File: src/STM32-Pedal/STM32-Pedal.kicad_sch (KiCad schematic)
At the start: 15 parts, among them J1 AudioJack2, U1 OPA134, U2 OPA134, U3 STM32H743ZITx

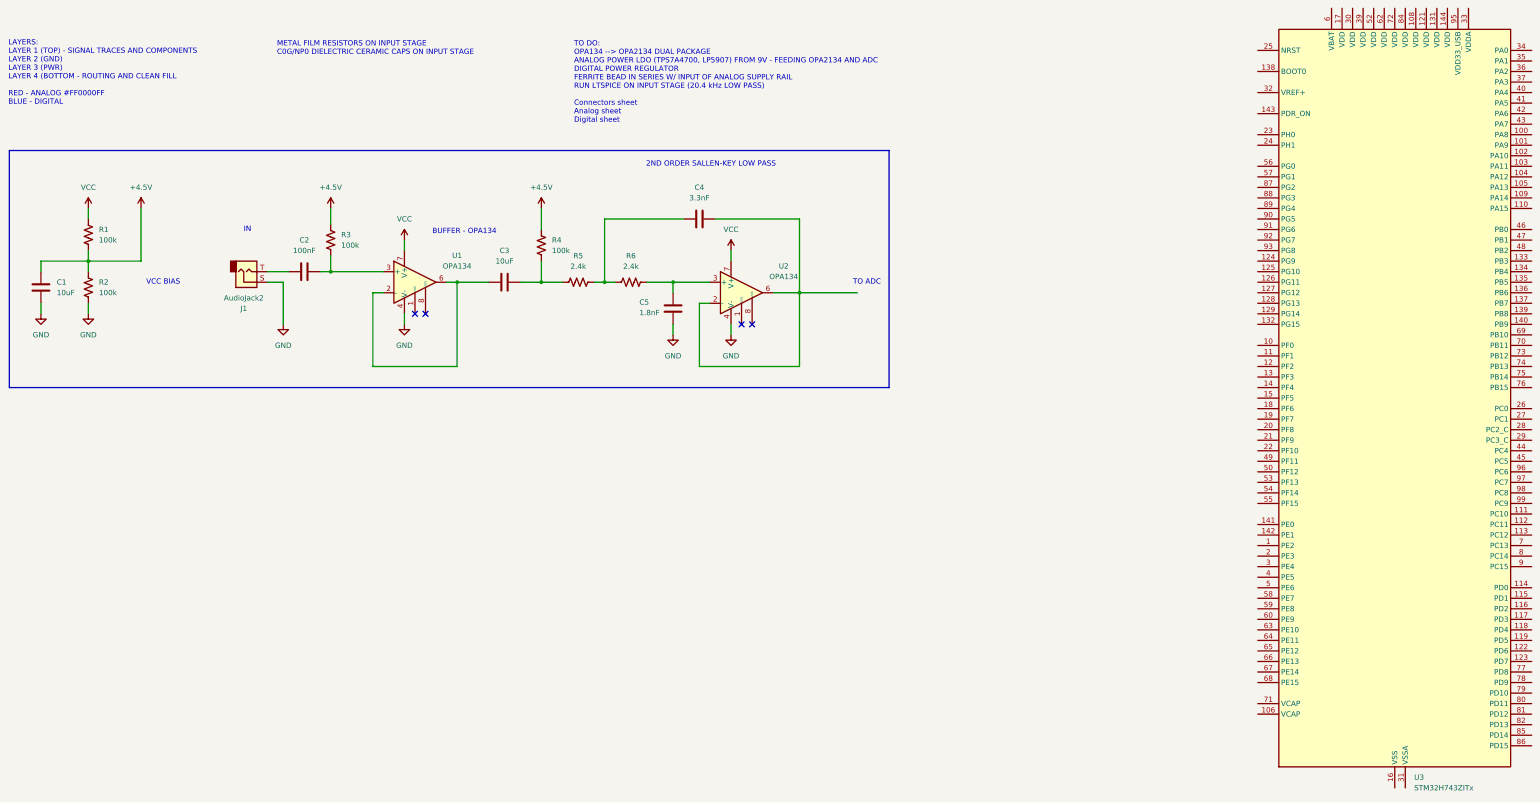
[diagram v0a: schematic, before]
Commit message: Schematic: codec, power, hierarchical sheets
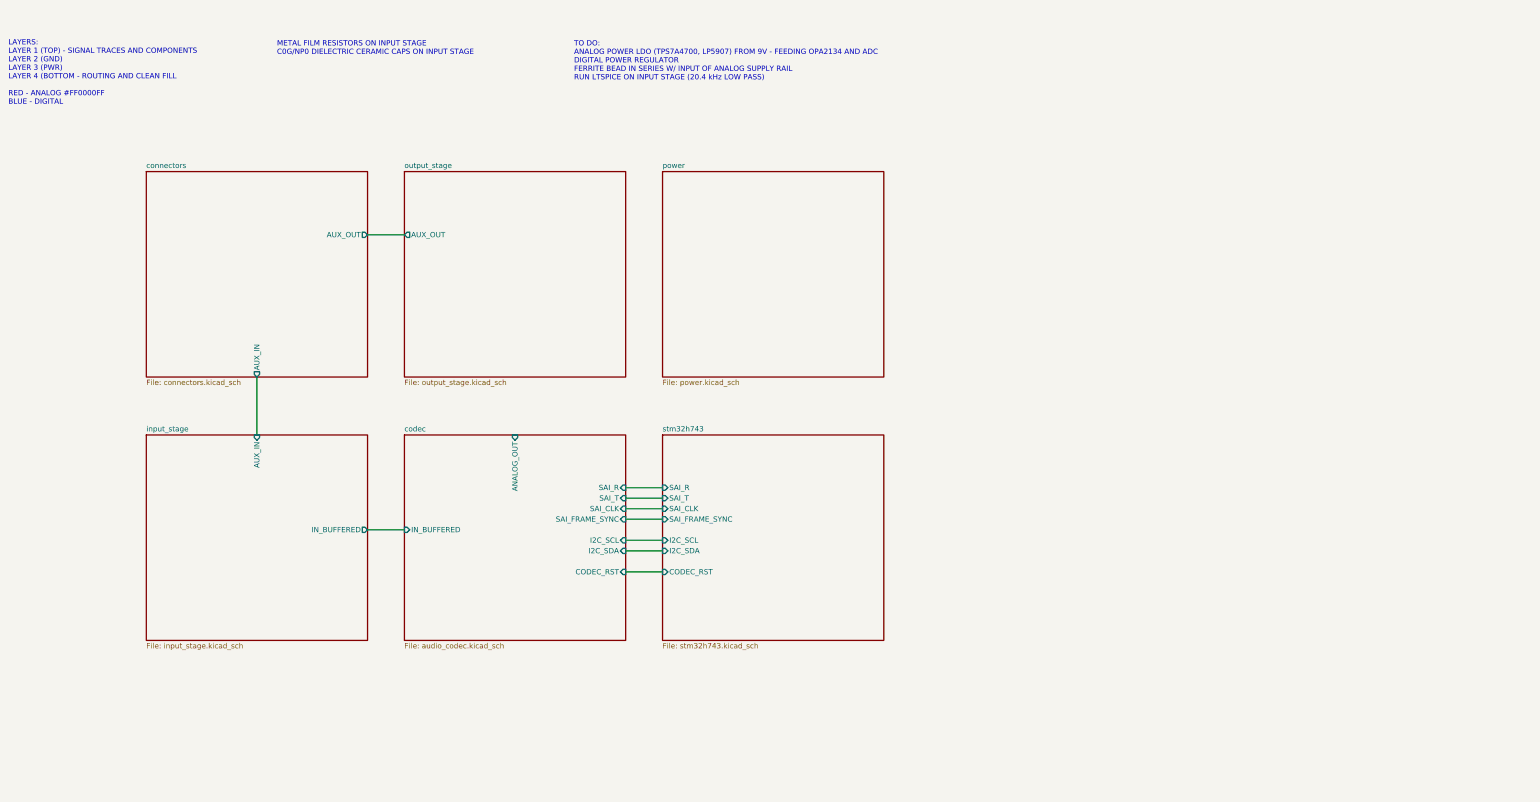
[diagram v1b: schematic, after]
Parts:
- removed C1, C3: 10uF, symbol Device:C
- removed C2: 100nF, symbol Device:C
- removed C4: 3.3nF, symbol Device:C
- removed C5: 1.8nF, symbol Device:C
- removed J1: AudioJack2, Connector_Audio:Jack_6.35mm_Neutrik_NMJ4HFD2_Horizontal, symbol Connector_Audio:AudioJack2
- removed R1, R2, R3, R4: 100k, symbol Device:R_US
- removed R5, R6: 2.4k, symbol Device:R_US
- removed U1, U2: OPA134, Package_SON:Texas_S-PVSON-N10, symbol Amplifier_Operational:OPA134
- removed U3: STM32H743ZITx, Package_QFP:LQFP-144_20x20mm_P0.5mm, symbol MCU_ST_STM32H7:STM32H743ZITx
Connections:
- no-connect marks 4 -> 0
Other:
- added sheet codec (audio_codec.kicad_sch)
- added sheet connectors (connectors.kicad_sch)
- added sheet input_stage (input_stage.kicad_sch)
- added sheet output_stage (output_stage.kicad_sch)
- added sheet power (power.kicad_sch)
- added sheet stm32h743 (stm32h743.kicad_sch)
- note added: "TO DO: ANALOG POWER LDO (TPS7A4700, LP5907) FROM 9V - FEEDING OPA2134 AND ADC DIGITAL POWER REGULATOR FERRITE BEAD IN SERIES W/ INPUT OF ANALOG SUPPLY RAIL RUN LTSPICE ON INPUT STAGE (20.4 kHz LOW PASS)"
- note removed: "2ND ORDER SALLEN-KEY LOW PASS"
- note removed: "BUFFER - OPA134"
- note removed: "IN"
- note removed: "TO ADC"
- note removed: "TO DO: OPA134 --> OPA2134 DUAL PACKAGE ANALOG POWER LDO (TPS7A4700, LP5907) FROM 9V - FEEDING OPA2134 AND ADC DIGITAL POWER REGULATOR FERRITE BEAD IN SERIES W/ INPUT OF ANALOG SUPPLY RAIL RUN LTSPICE ON INPUT STAGE (20.4 kHz LOW PASS) Connectors sheet Analog sheet Digital sheet"
- note removed: "VCC BIAS"

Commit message: Schematic - 3.3v, stm32 progress, usb-c
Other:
- sheet connectors ports: added USB_DM, USB_DP, USB_VBUS; removed none
- sheet output_stage ports: added ANALOG_OUT; removed none
- sheet stm32h743 ports: added USB_DM, USB_DP, USB_VBUS; removed none
- note added: "PCB LAYOUT NOTES: USB Differentials - target 90 ohms differential impedance"
- note added: "TO DO: FERRITE BEAD IN SERIES W/ INPUT OF ANALOG SUPPLY RAIL RUN LTSPICE ON INPUT STAGE (20.4 kHz LOW PASS) BYPASS RELAY"
- note removed: "TO DO: ANALOG POWER LDO (TPS7A4700, LP5907) FROM 9V - FEEDING OPA2134 AND ADC DIGITAL POWER REGULATOR FERRITE BEAD IN SERIES W/ INPUT OF ANALOG SUPPLY RAIL RUN LTSPICE ON INPUT STAGE (20.4 kHz LOW PASS)"
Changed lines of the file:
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@@
 		)
 	)
-	(text "TO DO:\nANALOG POWER LDO (TPS7A4700, LP5907) FROM 9V - FEEDING OPA2134 AND ADC\nDIGITAL POWER REGULATOR\nFERRITE BEAD IN SERIES W/ INPUT OF ANALOG SUPPLY RAIL\nRUN LTSPICE ON INPUT STAGE (20.4 kHz LOW PASS)"
+	(text "PCB LAYOUT NOTES:\nUSB Differentials - target 90 ohms differential impedance"
+		(exclude_from_sim no)
+		(at 22.098 185.42 0)
+		(effects
+			(font
+				(size 1.27 1.27)
+			)
+			(justify left top)
+		)
+	)
+	(text "TO DO:\nFERRITE BEAD IN SERIES W/ INPUT OF ANALOG SUPPLY RAIL\nRUN LTSPICE ON INPUT STAGE (20.4 kHz LOW PASS)\nBYPASS RELAY"
 		(exclude_from_sim no)
 		(at 153.924 19.304 0)
@@
 	(wire
 		(pts
+			(xy 146.05 100.33) (xy 146.05 114.3)
+		)
+		(stroke
+			(width 0)
+			(type default)
+		)
+	)
+	(wire
+		(pts
+			(xy 100.33 105.41) (xy 195.58 105.41)
+		)
+		(stroke
+			(width 0)
+			(type default)
+		)
+	)
+	(wire
+		(pts
 			(xy 166.37 132.08) (xy 175.26 132.08)
 		)
@@
 	(wire
 		(pts
-			(xy 104.14 137.16) (xy 113.03 137.16)
+			(xy 104.14 138.43) (xy 113.03 138.43)
 		)
 		(stroke
@@
 	(wire
 		(pts
+			(xy 193.04 106.68) (xy 193.04 114.3)
+		)
+		(stroke
+			(width 0)
+			(type default)
+		)
+	)
+	(wire
+		(pts
 			(xy 166.37 147.32) (xy 175.26 147.32)
 		)
@@
 	(wire
 		(pts
+			(xy 95.25 107.95) (xy 190.5 107.95)
+		)
+		(stroke
+			(width 0)
+			(type default)
+		)
+	)
+	(wire
+		(pts
+			(xy 195.58 105.41) (xy 195.58 114.3)
+		)
+		(stroke
+			(width 0)
+			(type default)
+		)
+	)
+	(wire
+		(pts
 			(xy 166.37 142.24) (xy 175.26 142.24)
 		)
@@
 	(wire
 		(pts
+			(xy 190.5 107.95) (xy 190.5 114.3)
+		)
+		(stroke
+			(width 0)
+			(type default)
+		)
+	)
+	(wire
+		(pts
+			(xy 100.33 100.33) (xy 100.33 105.41)
+		)
+		(stroke
+			(width 0)
+			(type default)
+		)
+	)
+	(wire
+		(pts
 			(xy 166.37 127) (xy 175.26 127)
 		)
@@
 	(wire
 		(pts
-			(xy 104.14 66.04) (xy 113.03 66.04)
-		)
-		(stroke
-			(width 0)
-			(type default)
-		)
-	)
-	(wire
-		(pts
-			(xy 77.47 100.33) (xy 77.47 114.3)
+			(xy 104.14 76.2) (xy 113.03 76.2)
+		)
+		(stroke
+			(width 0)
+			(type default)
+		)
+	)
+	(wire
+		(pts
+			(xy 95.25 100.33) (xy 95.25 107.95)
+		)
+		(stroke
+			(width 0)
+			(type default)
+		)
+	)
+	(wire
+		(pts
+			(xy 82.55 100.33) (xy 82.55 114.3)
+		)
+		(stroke
+			(width 0)
+			(type default)
+		)
+	)
+	(wire
+		(pts
+			(xy 97.79 106.68) (xy 193.04 106.68)
+		)
+		(stroke
+			(width 0)
+			(type default)
+		)
+	)
+	(wire
+		(pts
+			(xy 97.79 100.33) (xy 97.79 106.68)
 		)
 		(stroke
@@
 		)
 		(pin "IN_BUFFERED" input
-			(at 113.03 137.16 180)
-			(effects
-				(font
-					(size 1.27 1.27)
-				)
-				(justify left)
-			)
-		)
-		(pin "ANALOG_OUT" input
-			(at 139.7 114.3 90)
+			(at 113.03 138.43 180)
+			(effects
+				(font
+					(size 1.27 1.27)
+				)
+				(justify left)
+			)
+		)
+		(pin "ANALOG_OUT" output
+			(at 146.05 114.3 90)
 			(effects
 				(font
@@
 		)
 		(pin "IN_BUFFERED" output
-			(at 104.14 137.16 0)
+			(at 104.14 138.43 0)
 			(effects
 				(font
@@
 		)
 		(pin "AUX_IN" input
-			(at 77.47 114.3 90)
+			(at 82.55 114.3 90)
 			(effects
 				(font
@@
 		)
 		(pin "AUX_IN" output
-			(at 77.47 100.33 270)
-			(effects
-				(font
-					(size 1.27 1.27)
-				)
-				(justify left)
-			)
-		)
-		(pin "AUX_OUT" output
-			(at 104.14 66.04 0)
-			(effects
-				(font
-					(size 1.27 1.27)
-				)
-				(justify right)
+			(at 82.55 100.33 270)
+			(effects
+				(font
+					(size 1.27 1.27)
+				)
+				(justify left)
+			)
+		)
+		(pin "AUX_OUT" input
+			(at 104.14 76.2 0)
+			(effects
+				(font
+					(size 1.27 1.27)
+				)
+				(justify right)
+			)
+		)
+		(pin "USB_DM" output
+			(at 97.79 100.33 270)
+			(effects
+				(font
+					(size 1.27 1.27)
+				)
+				(justify left)
+			)
+		)
+		(pin "USB_DP" output
+			(at 95.25 100.33 270)
+			(effects
+				(font
+					(size 1.27 1.27)
+				)
+				(justify left)
+			)
+		)
+		(pin "USB_VBUS" output
+			(at 100.33 100.33 270)
+			(effects
+				(font
+					(size 1.27 1.27)
+				)
+				(justify left)
 			)
 		)
@@
 		)
 		(pin "AUX_OUT" output
-			(at 113.03 66.04 180)
+			(at 113.03 76.2 180)
+			(effects
+				(font
+					(size 1.27 1.27)
+				)
+				(justify left)
+			)
+		)
+		(pin "ANALOG_OUT" input
+			(at 146.05 100.33 270)
 			(effects
 				(font
@@
 			)
 		)
+		(pin "USB_DM" input
+			(at 193.04 114.3 90)
+			(effects
+				(font
+					(size 1.27 1.27)
+				)
+				(justify right)
+			)
+		)
+		(pin "USB_DP" input
+			(at 190.5 114.3 90)
+			(effects
+				(font
+					(size 1.27 1.27)
+				)
+				(justify right)
+			)
+		)
+		(pin "USB_VBUS" input
+			(at 195.58 114.3 90)
+			(effects
+				(font
+					(size 1.27 1.27)
+				)
+				(justify right)
+			)
+		)
